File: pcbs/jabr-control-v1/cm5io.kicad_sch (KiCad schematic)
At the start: 20 parts, among them J10001 ARJM11D7-502-AB-EW2, J10002 TYPE-C-31-M-12, J1001 48406-0003, U1001 AP22653FDZ-7, U1002 PESD4USB3BTTS-QX, U1003 PESD4USB3BTTS-QX, U1004 PESD4USB3BTTS-QX, U1005 PESD4USB3BTTS-QX, U2401 PESD4USB3BTTS-QX, U2402 PESD4USB3BTTS-QX

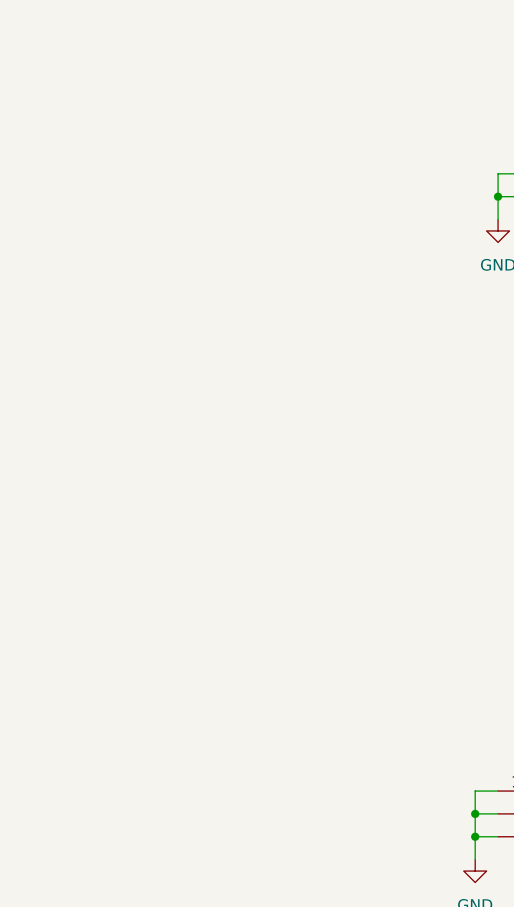
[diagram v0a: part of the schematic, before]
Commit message: Updated FH12-22S-0.5SH footprints
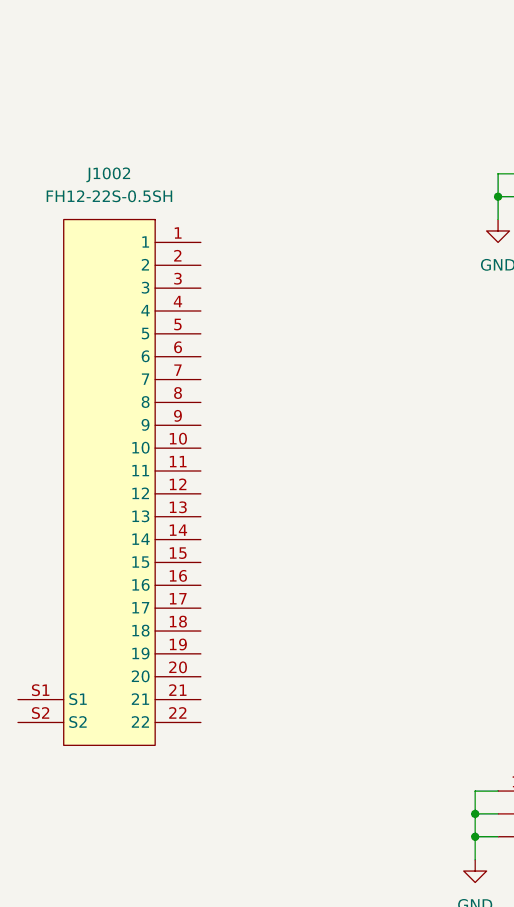
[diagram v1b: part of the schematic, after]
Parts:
- added J1002: FH12-22S-0.5SH, project_footprints:Hirose_FH12-22S-0.5SH_1x22-1MP_P0.50mm_Horizontal, symbol CONN-FPC:FH12-22S-0.5SH
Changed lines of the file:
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@@
+	)
+	(symbol
+		(lib_id "CONN-FPC:FH12-22S-0.5SH")
+		(at -17.78 88.9 0)
+		(mirror y)
+		(unit 1)
+		(exclude_from_sim no)
+		(in_bom yes)
+		(on_board yes)
+		(dnp no)
+		(fields_autoplaced yes)
+		(property "Reference" "J1002"
+			(at -17.78 83.82 0)
+			(effects
+				(font
+					(size 1.27 1.27)
+				)
+			)
+		)
+		(property "Value" "FH12-22S-0.5SH"
+			(at -17.78 86.36 0)
+			(effects
+				(font
+					(size 1.27 1.27)
+				)
+			)
+		)
+		(property "Footprint" "project_footprints:Hirose_FH12-22S-0.5SH_1x22-1MP_P0.50mm_Horizontal"
+			(at -19.05 152.4 0)
+			(effects
+				(font
+					(size 1.27 1.27)
+				)
+				(hide yes)
+			)
+		)
+		(property "Datasheet" "https://www.mouser.co.uk/datasheet/3/731/1/FH12_22S_0.5SH_55_CL0586_0532_7_55_2DDrawing_0000987484.pdf"
+			(at -17.78 149.86 0)
+			(effects
+				(font
+					(size 1.27 1.27)
+				)
+				(hide yes)
+			)
+		)
+		(property "Description" ""
+			(at -17.78 88.9 0)
+			(effects
+				(font
+					(size 1.27 1.27)
+				)
+				(hide yes)
+			)
+		)
+		(property "Field6" ""
+			(at -17.78 88.9 0)
+			(effects
+				(font
+					(size 1.27 1.27)
+				)
+				(hide yes)
+			)
+		)
+		(property "Field7" ""
+			(at -17.78 88.9 0)
+			(effects
+				(font
+					(size 1.27 1.27)
+				)
+				(hide yes)
+			)
+		)
+		(property "Part Description" ""
+			(at -17.78 88.9 0)
+			(effects
+				(font
+					(size 1.27 1.27)
+				)
+				(hide yes)
+			)
+		)
+		(pin "7"
+		)
+		(pin "22"
+		)
+		(pin "4"
+		)
+		(pin "2"
+		)
+		(pin "15"
+		)
+		(pin "S2"
+		)
+		(pin "12"
+		)
+		(pin "6"
+		)
+		(pin "1"
+		)
+		(pin "9"
+		)
+		(pin "16"
+		)
+		(pin "14"
+		)
+		(pin "17"
+		)
+		(pin "13"
+		)
+		(pin "3"
+		)
+		(pin "5"
+		)
+		(pin "8"
+		)
+		(pin "18"
+		)
+		(pin "11"
+		)
+		(pin "19"
+		)
+		(pin "20"
+		)
+		(pin "21"
+		)
+		(pin "10"
+		)
+		(pin "S1"
+		)
+		(instances
+			(project "jabr-control-v1"
+				(path "/f91ec272-d09a-4038-bbbb-962739a92c51/adc0b005-3094-4656-96e7-4ee9fb2ab719"
+					(reference "J1002")
+					(unit 1)
+				)
+			)
+		)
 	)
 	(symbol
